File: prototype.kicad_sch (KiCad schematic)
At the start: 7 parts, among them CON1 SNES-CONN, IC1 SN74LVC4245A, IC2 SN74LVC4245A, IC3 SN74LVC4245A, IC4 SN74LVC4245A

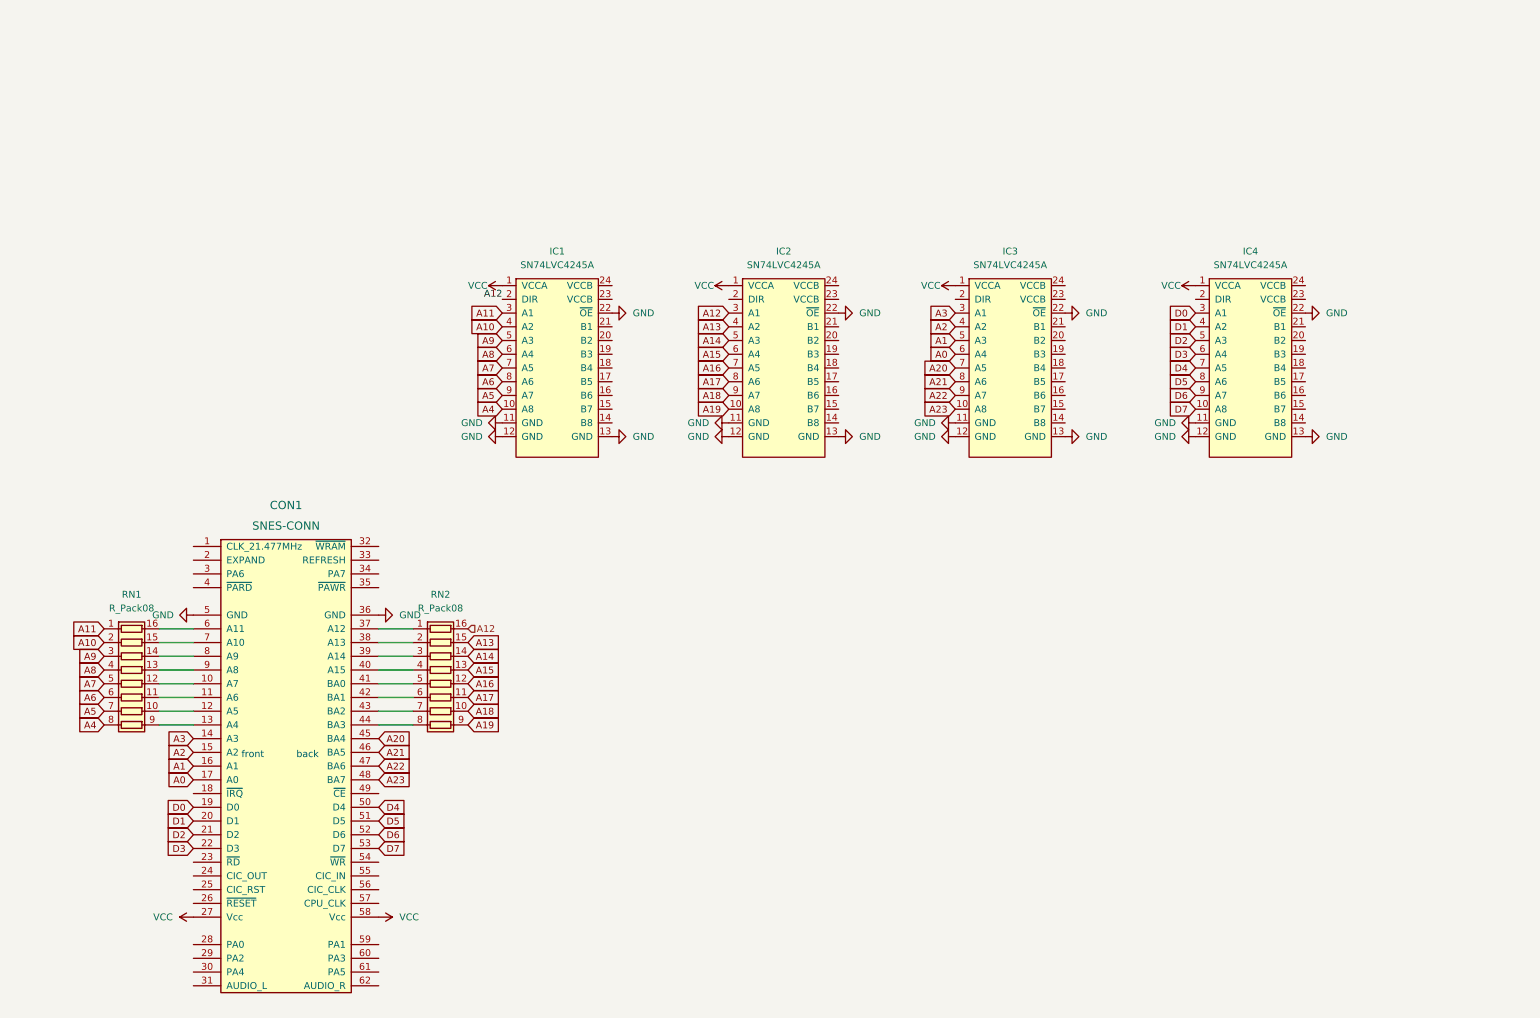
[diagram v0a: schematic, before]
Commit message: Add resistor networks in between edge connectors and level shifters
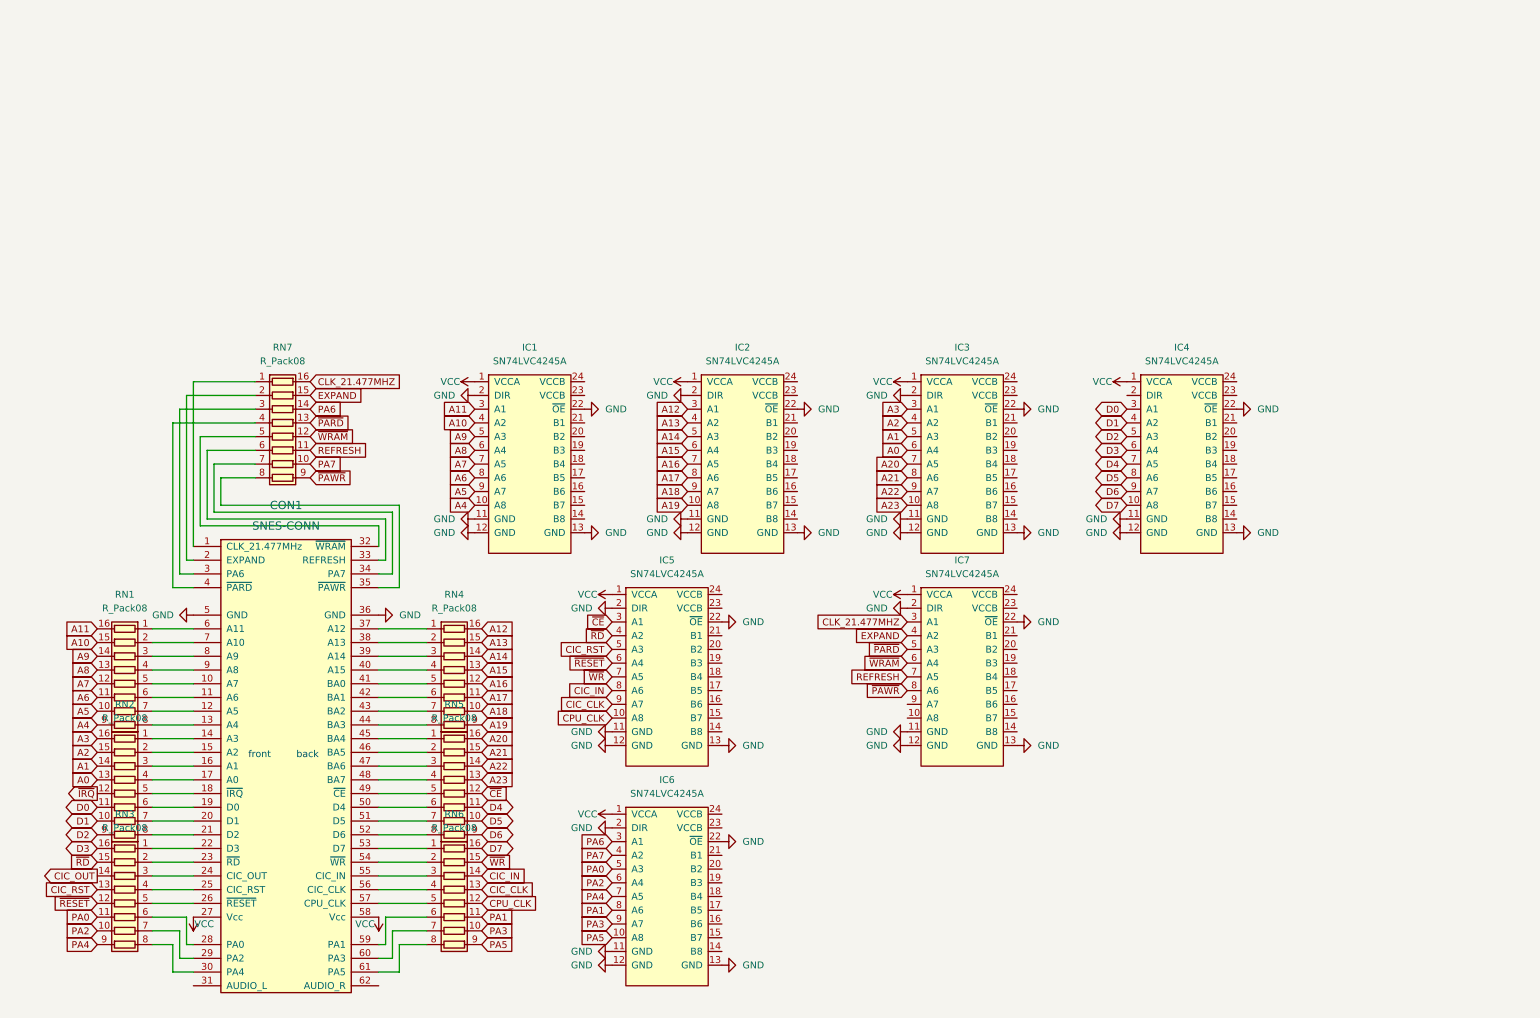
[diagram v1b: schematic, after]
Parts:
- added IC5, IC6, IC7: SN74LVC4245A, Package_SO:SOIC-24W_7.5x15.4mm_P1.27mm, symbol sn74lvc4245a:SN74LVC4245A
- added RN2, RN3, RN5, RN6, RN7: R_Pack08, Package_SO:SOIC-16_3.9x9.9mm_P1.27mm, symbol Device:R_Pack08
- renumbered RN2 to RN4
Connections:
- net A0: now also RN2.13 (R4.2); no longer CON1.17 (A0)
- net A1: now also RN2.14 (R3.2); no longer CON1.16 (A1)
- net A10: now also RN1.15 (R2.2); no longer RN1.2 (R2.1)
- net A11: now also RN1.16 (R1.2); no longer RN1.1 (R1.1)
- net A12: no longer IC1.2 (DIR)
- net A2: now also RN2.15 (R2.2); no longer CON1.15 (A2)
- net A20: now also RN5.16 (R1.2); no longer CON1.45 (BA4)
- net A21: now also RN5.15 (R2.2); no longer CON1.46 (BA5)
- net A22: now also RN5.14 (R3.2); no longer CON1.47 (BA6)
- net A23: now also RN5.13 (R4.2); no longer CON1.48 (BA7)
- net A3: now also RN2.16 (R1.2); no longer CON1.14 (A3)
- net A4: now also RN1.9 (R8.2); no longer RN1.8 (R8.1)
- net A5: now also RN1.10 (R7.2); no longer RN1.7 (R7.1)
- net A6: now also RN1.11 (R6.2); no longer RN1.6 (R6.1)
- net A7: now also RN1.12 (R5.2); no longer RN1.5 (R5.1)
- net A8: now also RN1.13 (R4.2); no longer RN1.4 (R4.1)
- net A9: now also RN1.14 (R3.2); no longer RN1.3 (R3.1)
- net D0: now also RN2.11 (R6.2); no longer CON1.19 (D0)
- net D1: now also RN2.10 (R7.2); no longer CON1.20 (D1)
- net D2: now also RN2.9 (R8.2); no longer CON1.21 (D2)
- net D3: now also RN3.16 (R1.2); no longer CON1.22 (D3)
- net D4: now also RN5.11 (R6.2); no longer CON1.50 (D4)
- net D5: now also RN5.10 (R7.2); no longer CON1.51 (D5)
- net D6: now also RN5.9 (R8.2); no longer CON1.52 (D6)
- net D7: now also RN6.16 (R1.2); no longer CON1.53 (D7)
- net GND: now also IC1.2 (DIR), IC2.2 (DIR), IC3.2 (DIR), IC5.11 (GND), IC5.12 (GND), IC5.13 (GND), IC5.2 (DIR), IC5.22 (~{OE}), IC6.11 (GND), IC6.12 (GND), IC6.13 (GND), IC6.2 (DIR), IC6.22 (~{OE}), IC7.11 (GND), IC7.12 (GND), IC7.13 (GND), IC7.2 (DIR), IC7.22 (~{OE})
- net VCC: now also IC5.1 (VCCA), IC6.1 (VCCA), IC7.1 (VCCA)
- net at CON1.1 (CLK_21.477MHz): now also RN7.1 (R1.1)
- net at CON1.10 (A7): now also RN1.5 (R5.1); no longer RN1.12 (R5.2)
- net at CON1.11 (A6): now also RN1.6 (R6.1); no longer RN1.11 (R6.2)
- net at CON1.12 (A5): now also RN1.7 (R7.1); no longer RN1.10 (R7.2)
- net at CON1.13 (A4): now also RN1.8 (R8.1); no longer RN1.9 (R8.2)
- net at CON1.18 (~{IRQ}): now also RN2.5 (R5.1)
- net at CON1.2 (EXPAND): now also RN7.2 (R2.1)
- net at CON1.23 (~{RD}): now also RN3.2 (R2.1)
- net at CON1.24 (CIC_OUT): now also RN3.3 (R3.1)
- net at CON1.25 (CIC_RST): now also RN3.4 (R4.1)
- net at CON1.26 (~{RESET}): now also RN3.5 (R5.1)
- net at CON1.28 (PA0): now also RN3.6 (R6.1)
- net at CON1.29 (PA2): now also RN3.7 (R7.1)
- net at CON1.3 (PA6): now also RN7.3 (R3.1)
- net at CON1.30 (PA4): now also RN3.8 (R8.1)
- net at CON1.32 (~{WRAM}): now also RN7.5 (R5.1)
- net at CON1.33 (REFRESH): now also RN7.6 (R6.1)
- net at CON1.34 (PA7): now also RN7.7 (R7.1)
- net at CON1.35 (~{PAWR}): now also RN7.8 (R8.1)
- net at CON1.4 (~{PARD}): now also RN7.4 (R4.1)
- net at CON1.49 (~{CE}): now also RN5.5 (R5.1)
- net at CON1.54 (~{WR}): now also RN6.2 (R2.1)
- net at CON1.55 (CIC_IN): now also RN6.3 (R3.1)
- net at CON1.56 (CIC_CLK): now also RN6.4 (R4.1)
- net at CON1.57 (CPU_CLK): now also RN6.5 (R5.1)
- net at CON1.59 (PA1): now also RN6.6 (R6.1)
- net at CON1.6 (A11): now also RN1.1 (R1.1); no longer RN1.16 (R1.2)
- net at CON1.60 (PA3): now also RN6.7 (R7.1)
- net at CON1.61 (PA5): now also RN6.8 (R8.1)
- net at CON1.7 (A10): now also RN1.2 (R2.1); no longer RN1.15 (R2.2)
- net at CON1.8 (A9): now also RN1.3 (R3.1); no longer RN1.14 (R3.2)
- net at CON1.9 (A8): now also RN1.4 (R4.1); no longer RN1.13 (R4.2)
- new net: CON1.14 (A3), RN2.1 (R1.1)
- new net: CON1.15 (A2), RN2.2 (R2.1)
- new net: CON1.16 (A1), RN2.3 (R3.1)
- new net: CON1.17 (A0), RN2.4 (R4.1)
- new net: CON1.19 (D0), RN2.6 (R6.1)
- new net: CON1.20 (D1), RN2.7 (R7.1)
- new net: CON1.21 (D2), RN2.8 (R8.1)
- new net: CON1.22 (D3), RN3.1 (R1.1)
- new net: CON1.45 (BA4), RN5.1 (R1.1)
- new net: CON1.46 (BA5), RN5.2 (R2.1)
- new net: CON1.47 (BA6), RN5.3 (R3.1)
- new net: CON1.48 (BA7), RN5.4 (R4.1)
- new net: CON1.50 (D4), RN5.6 (R6.1)
- new net: CON1.51 (D5), RN5.7 (R7.1)
- new net: CON1.52 (D6), RN5.8 (R8.1)
- new net: CON1.53 (D7), RN6.1 (R1.1)
- new net CIC_CLK: IC5.9 (A7), RN6.13 (R4.2)
- new net CIC_IN: IC5.8 (A6), RN6.14 (R3.2)
- new net CIC_OUT: RN3.14 (R3.2)
- new net CIC_RST: IC5.5 (A3), RN3.13 (R4.2)
- new net CLK_21.477MHZ: IC7.3 (A1), RN7.16 (R1.2)
- new net CPU_CLK: IC5.10 (A8), RN6.12 (R5.2)
- new net EXPAND: IC7.4 (A2), RN7.15 (R2.2)
- new net PA0: IC6.5 (A3), RN3.11 (R6.2)
- new net PA1: IC6.8 (A6), RN6.11 (R6.2)
- new net PA2: IC6.6 (A4), RN3.10 (R7.2)
- new net PA3: IC6.9 (A7), RN6.10 (R7.2)
- new net PA4: IC6.7 (A5), RN3.9 (R8.2)
- new net PA5: IC6.10 (A8), RN6.9 (R8.2)
- new net PA6: IC6.3 (A1), RN7.14 (R3.2)
- new net PA7: IC6.4 (A2), RN7.10 (R7.2)
- new net REFRESH: IC7.7 (A5), RN7.11 (R6.2)
- new net ~{CE}: IC5.3 (A1), RN5.12 (R5.2)
- new net ~{IRQ}: RN2.12 (R5.2)
- new net ~{PARD}: IC7.5 (A3), RN7.13 (R4.2)
- new net ~{PAWR}: IC7.8 (A6), RN7.9 (R8.2)
- new net ~{RD}: IC5.4 (A2), RN3.15 (R2.2)
- new net ~{RESET}: IC5.6 (A4), RN3.12 (R5.2)
- new net ~{WRAM}: IC7.6 (A4), RN7.12 (R5.2)
- new net ~{WR}: IC5.7 (A5), RN6.15 (R2.2)
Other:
- moved on the sheet: IC1, IC2, IC3, IC4, RN1, RN4

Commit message: Add 3V3 voltage regulator
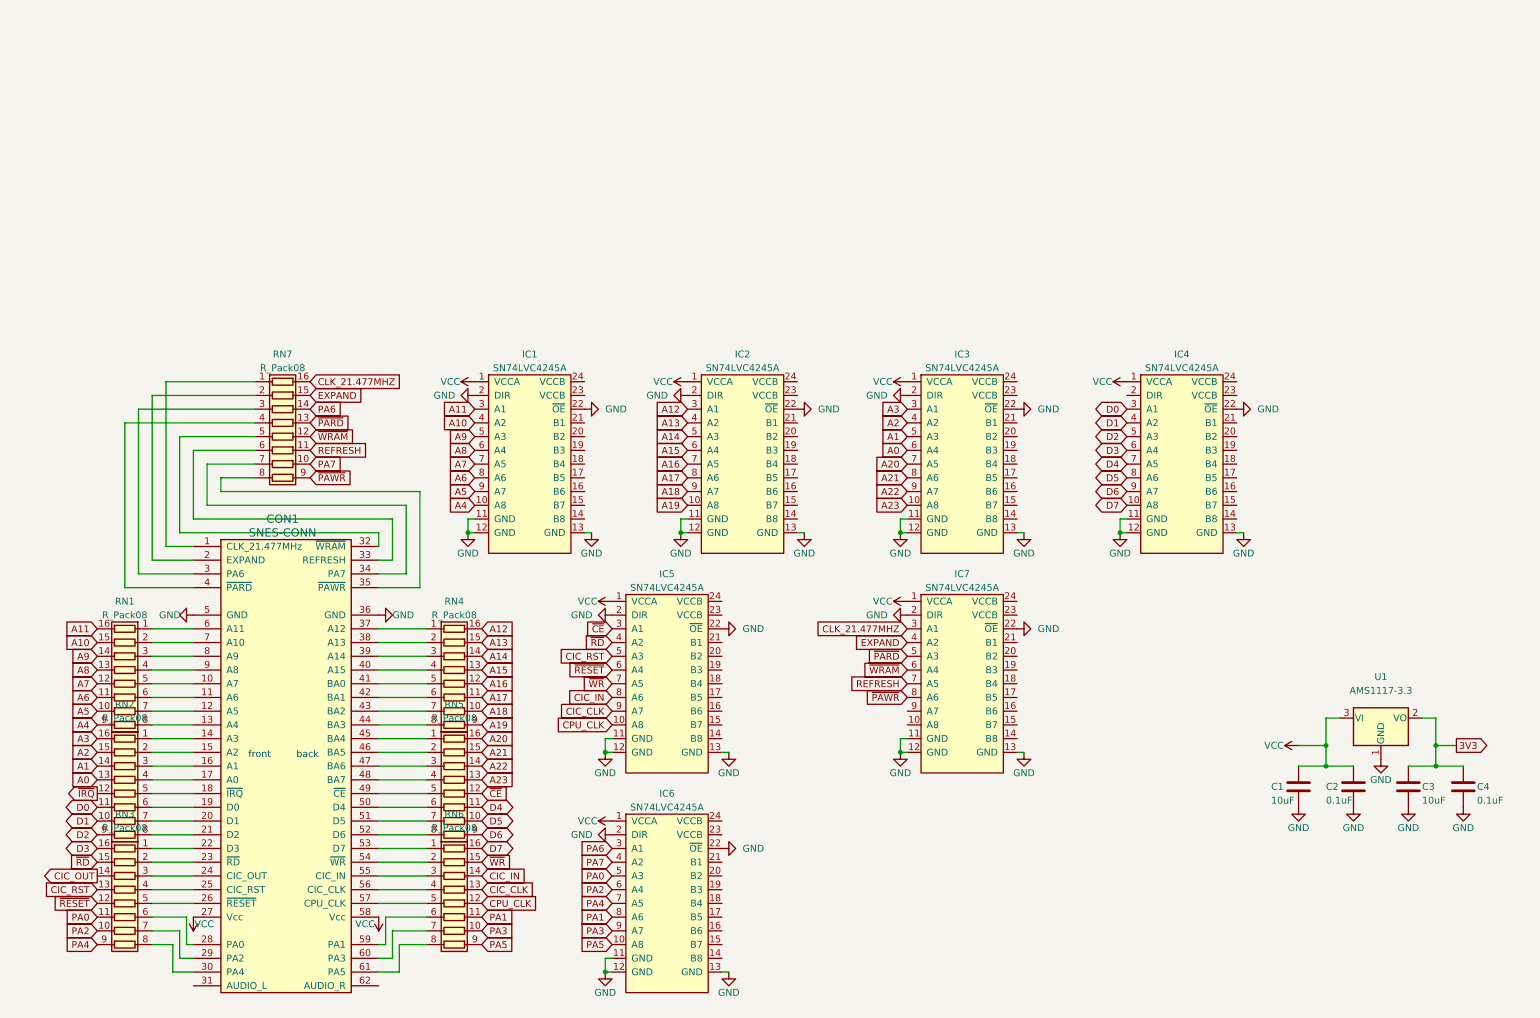
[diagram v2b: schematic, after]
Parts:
- added C1, C3: 10uF, symbol Device:C
- added C2, C4: 0.1uF, symbol Device:C
- added U1: AMS1117-3.3, Package_TO_SOT_SMD:SOT-223-3_TabPin2, symbol Regulator_Linear:AMS1117-3.3
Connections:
- net GND: now also C1.2, C2.2, C3.2, C4.2, U1.1 (GND)
- net VCC: now also C1.1, C2.1, U1.3 (VI)
- new net 3V3: C3.1, C4.1, U1.2 (VO)
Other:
- moved on the sheet: IC5, IC6, IC7

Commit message: Added 1206 footprints to caps
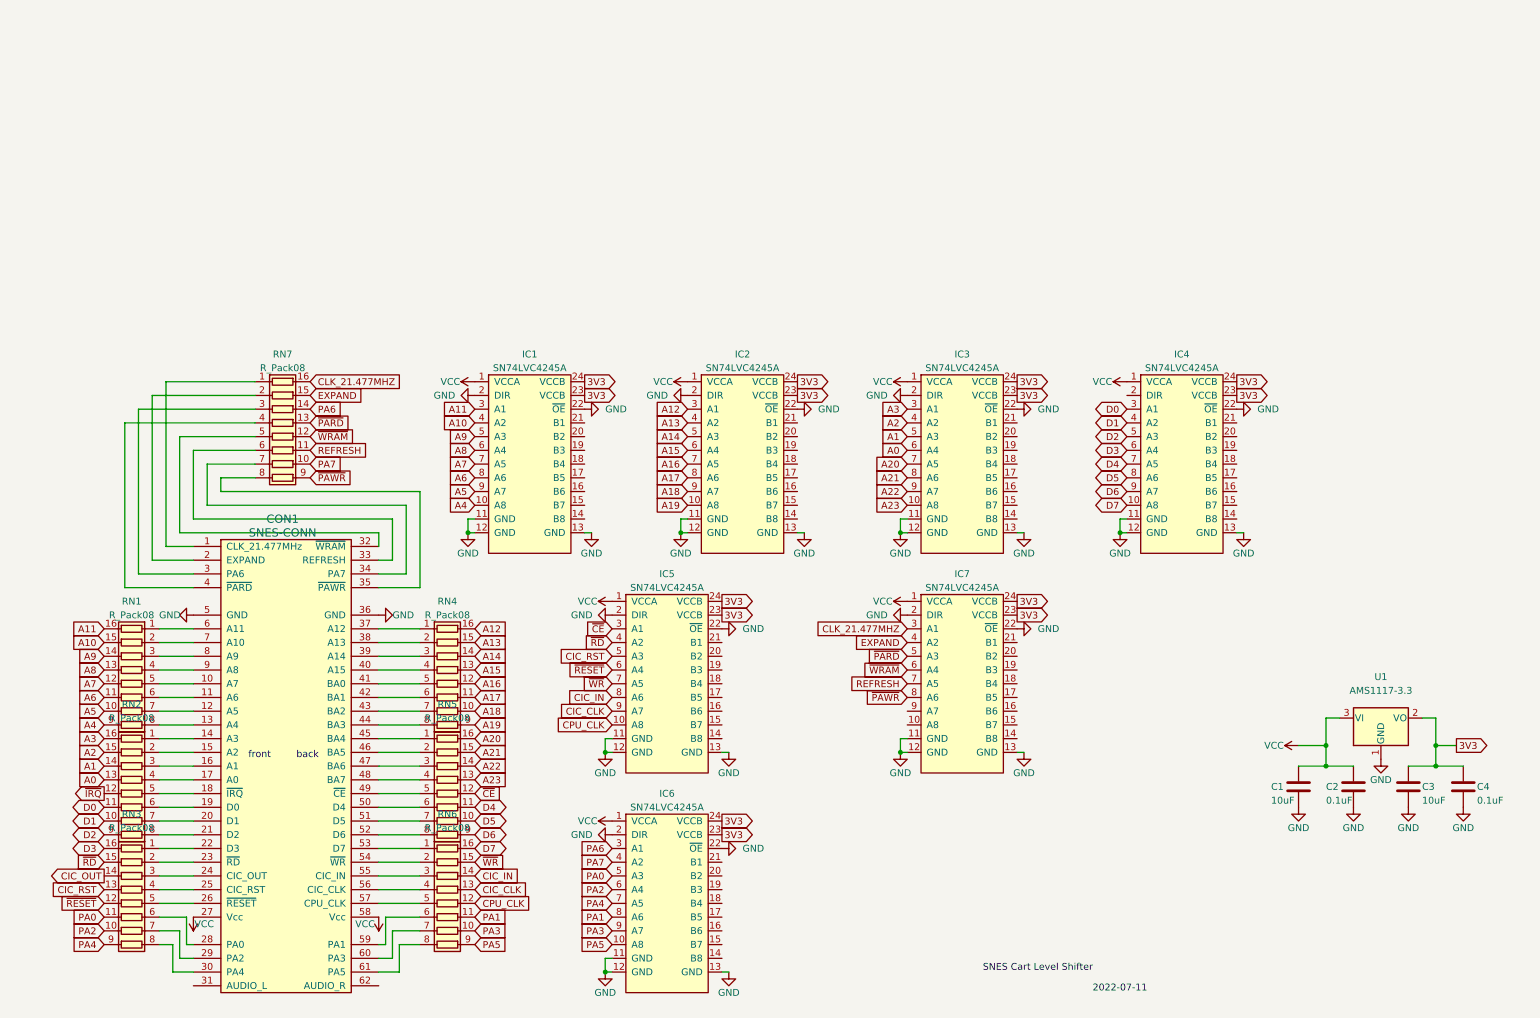
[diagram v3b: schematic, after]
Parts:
- C1, C2, C3, C4: footprint (none) -> Capacitor_SMD:C_1206_3216Metric
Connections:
- net 3V3: now also IC1.23 (VCCB), IC1.24 (VCCB), IC2.23 (VCCB), IC2.24 (VCCB), IC3.23 (VCCB), IC3.24 (VCCB), IC4.23 (VCCB), IC4.24 (VCCB), IC5.23 (VCCB), IC5.24 (VCCB), IC6.23 (VCCB), IC6.24 (VCCB), IC7.23 (VCCB), IC7.24 (VCCB)
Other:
- note added: "2022-07-11"
- note added: "SNES Cart Level Shifter"
- moved on the sheet: RN1, RN2, RN3, RN4, RN5, RN6
